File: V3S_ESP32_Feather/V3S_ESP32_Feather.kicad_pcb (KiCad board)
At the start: 4 copper layers, 30.5 x 48.3 mm, 83 parts, among them J1 USB_B_Micro, J10 UART, J2 PWM, J3 CAM, J5 U.FL-R-SMT(01), J7 Micro_SD_Card_Det, J8 I2C, J9 I2C, U1 V3S, U2 MIC5504-1.2YM5, U3 MIC5501-3.0YM5, U4 ICM-20948, U5 ESP32-PICO-D4, U6 LT1963AxST-3.3, U7 BMP280, U8 MIC5504-1.8YM5, U9 MAX13030EETE, Y1 X1E0000210832, Y2 CC5V-T1A 32.768KHZ +-20PPM 12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

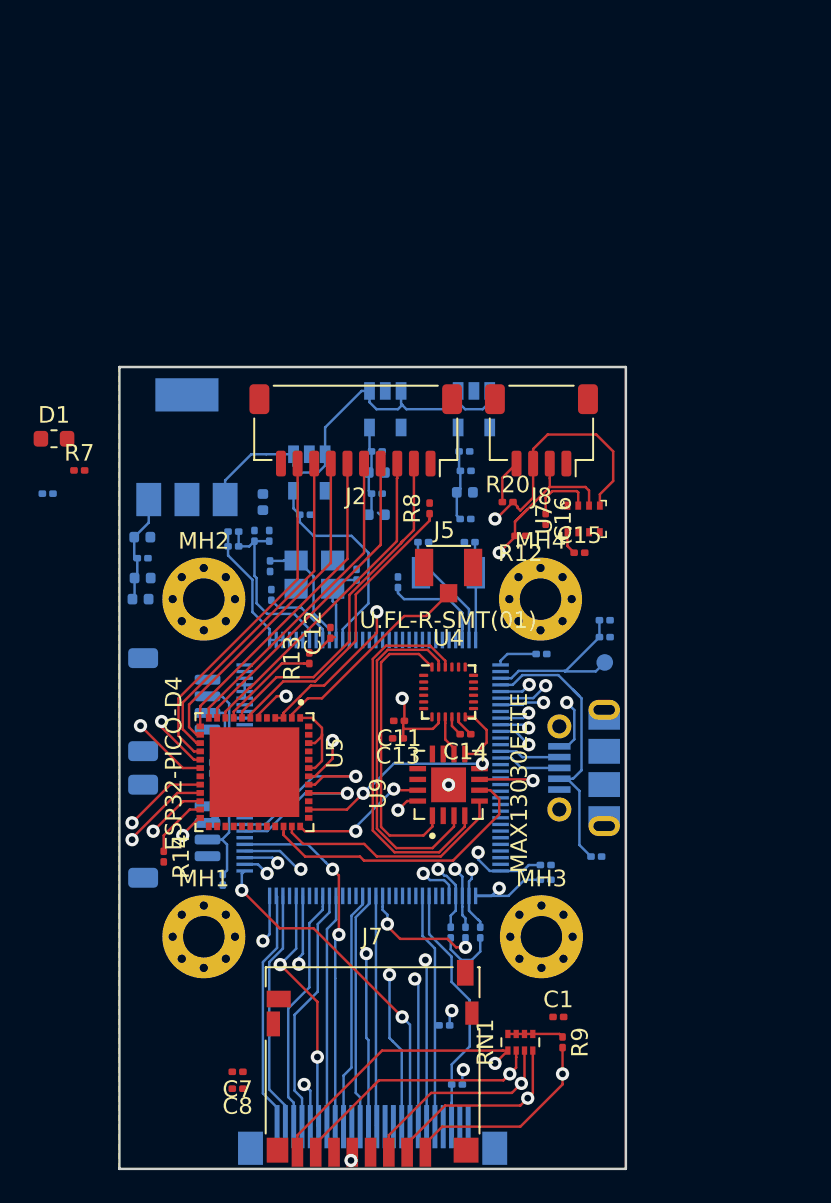
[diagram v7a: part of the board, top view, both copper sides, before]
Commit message: replace 3 ldo by 1, replace icm by mpu and progress on 2 layer
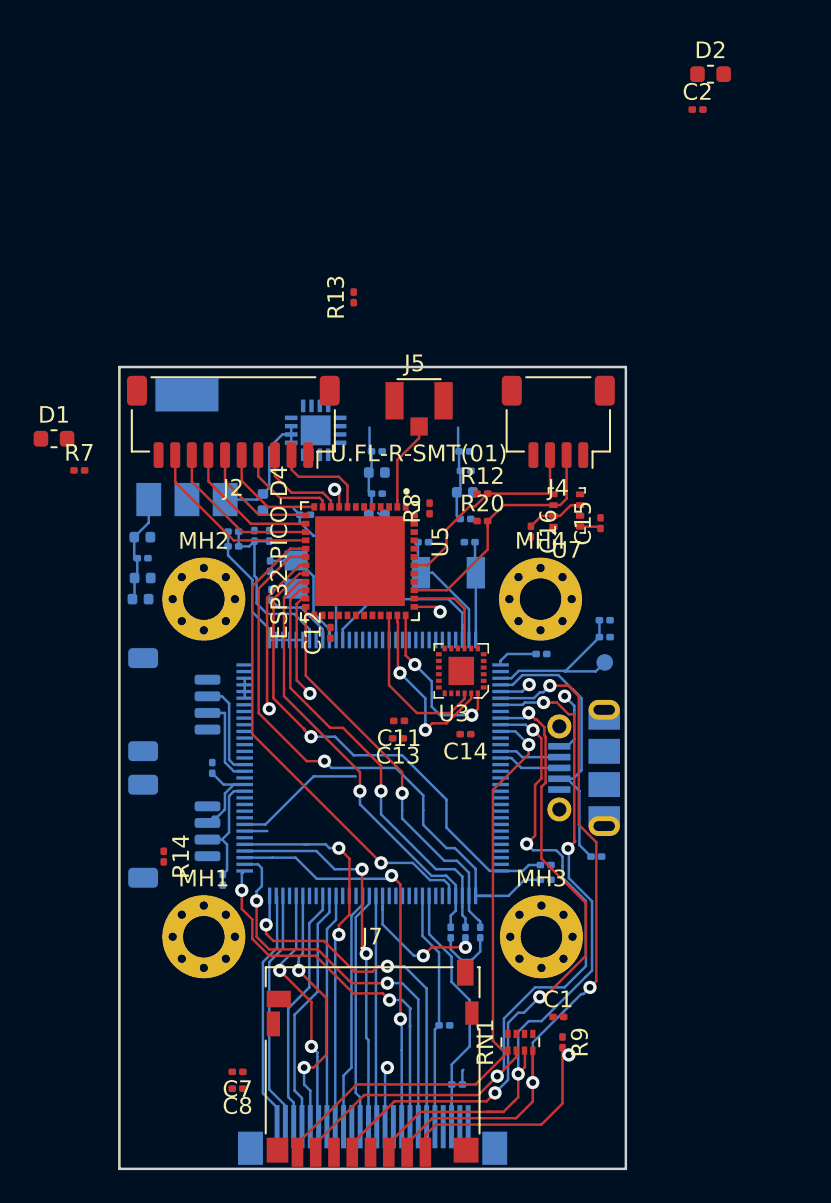
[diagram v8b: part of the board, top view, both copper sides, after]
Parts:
- removed J8: I2C, Connector_JST:JST_SH_SM04B-SRSS-TB_1x04-1MP_P1.00mm_Horizontal
- removed R1: 0, Resistor_SMD:R_0201_0603Metric
- removed U4: ICM-20948, Sensor_Motion:InvenSense_QFN-24_3x3mm_P0.4mm
- removed U8: MIC5504-1.8YM5, Package_TO_SOT_SMD:SOT-23-5
- removed U9: MAX13030EETE, MAX13035EETET:QFN65P400X400X80-17N
- added C2: 1uF, Capacitor_SMD:C_0201_0603Metric, F.Cu at (57.7, 4.83)
- added D2: D, Resistor_SMD:R_0603_1608Metric, F.Cu at (58.4, 2.70)
- added J4: I2C, Connector_JST:JST_SH_SM04B-SRSS-TB_1x04-1MP_P1.00mm_Horizontal, F.Cu at (49.3, 23.6)
- C11: value 0.1uF -> 10nF
- C13: value 1uF -> 0.1uF
- U2: value MIC5504-1.2YM5 -> ADP322ACPZ-145-R7; footprint Package_TO_SOT_SMD:SOT-23-5 -> QFN50P300X300X90-17N:QFN50P300X300X90-17N
- U3: value MIC5501-3.0YM5 -> MPU-9250_Obsolete; footprint Package_TO_SOT_SMD:SOT-23-5 -> digikey-footprints:QFN-24-1EP_3x3mm; moved to F.Cu
- moved R13 21.9 mm to (37.0, 16.1)
- moved U3 15.0 mm to (43.4, 38.6), turned to 180 degrees
- moved U5 14.2 mm to (37.3, 32.0)
- moved J5 10.2 mm to (40.9, 22.4)
- moved U2 9.61 mm to (34.7, 24.1), turned to 0 degrees
- moved J2 7.38 mm to (29.7, 23.6)
- moved R12 3.42 mm to (44.7, 27.9), turned to 0 degrees
- moved C15 2.18 mm to (51.8, 29.7), turned to 90 degrees
- moved R20 1.91 mm to (44.7, 29.6)
- moved C16 1.17 mm to (47.6, 30.2)
- moved U7 1.14 mm to (49.8, 29.0), turned to 180 degrees
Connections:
- net /IO25 renamed /WIFI, BT, RT/IO25
- net /IO26 renamed /WIFI, BT, RT/IO26
- net /IO27 renamed /WIFI, BT, RT/IO27
- net /IO32 renamed /WIFI, BT, RT/IO32
- net /IO33 renamed /WIFI, BT, RT/IO33
- net /IO34 renamed /WIFI, BT, RT/IO34
- net /IO35 renamed /WIFI, BT, RT/IO35
- net /SENSOR_VN renamed /WIFI, BT, RT/SENSOR_VN
- C11 pad 1: +1V8 -> +3V3
- C13 pad 1: +1V8 -> +3V3
- C5 pad 1: +BATT -> /PMIC Power Battery/VIN
- D1 pad 1: +BATT -> /PMIC Power Battery/VIN
- D1 pad 2: Net-(D1-Pad2) -> VBUS
- J3 pad 1: (no net) -> /All V3s input output/STROBE
- J3 pad 10: (no net) -> Net-(J3-Pad10)
- J7 pad 10: (no net) -> Net-(J7-Pad10)
- J7 pad 9: (no net) -> Net-(J7-Pad9)
- R12 pad 2: /SDA -> /WIFI, BT, RT/SCL
- R20 pad 2: /SCL -> /WIFI, BT, RT/SDA
- U1 pad 10: (no net) -> Net-(U1-Pad10)
- U1 pad 11: (no net) -> Net-(U1-Pad11)
- U1 pad 112: (no net) -> Net-(U1-Pad112)
- U1 pad 113: (no net) -> Net-(U1-Pad113)
- U1 pad 114: (no net) -> Net-(U1-Pad114)
- U1 pad 120: (no net) -> Net-(U1-Pad120)
- U1 pad 121: (no net) -> Net-(U1-Pad121)
- U1 pad 124: (no net) -> Net-(U1-Pad124)
- U1 pad 125: (no net) -> Net-(U1-Pad125)
- U1 pad 13: (no net) -> Net-(U1-Pad13)
- U1 pad 14: (no net) -> Net-(U1-Pad14)
- U1 pad 43: (no net) -> Net-(U1-Pad43)
- U1 pad 44: (no net) -> Net-(U1-Pad44)
- U1 pad 52: (no net) -> Net-(U1-Pad52)
- U1 pad 53: (no net) -> Net-(U1-Pad53)
- U1 pad 54: (no net) -> Net-(U1-Pad54)
- U1 pad 55: (no net) -> Net-(U1-Pad55)
- U1 pad 6: (no net) -> Net-(U1-Pad6)
- U1 pad 7: (no net) -> Net-(U1-Pad7)
- U1 pad 77: (no net) -> Net-(U1-Pad77)
- U1 pad 78: (no net) -> Net-(U1-Pad78)
- U1 pad 81: (no net) -> Net-(U1-Pad81)
- U1 pad 82: (no net) -> Net-(U1-Pad82)
- U1 pad 83: (no net) -> Net-(U1-Pad83)
- U1 pad 84: (no net) -> Net-(U1-Pad84)
- U1 pad 86: (no net) -> Net-(U1-Pad86)
- U1 pad 87: (no net) -> Net-(U1-Pad87)
- U1 pad 89: (no net) -> Net-(U1-Pad89)
- U1 pad 90: (no net) -> Net-(U1-Pad90)
- U1 pad 91: (no net) -> Net-(U1-Pad91)
- U1 pad 92: (no net) -> Net-(U1-Pad92)
- U2 pad 1: +BATT -> /PMIC Power Battery/VIN
- U2 pad 2: GND -> /PMIC Power Battery/VIN
- U2 pad 3: +BATT -> /PMIC Power Battery/VIN
- U2 pad 4: (no net) -> Net-(U2-Pad4)
- U2 pad 5: +1V2 -> +3V0
- U3 pad 1: +BATT -> +3V3
- U3 pad 2: GND -> Net-(U3-Pad2)
- U3 pad 3: +BATT -> Net-(U3-Pad3)
- U3 pad 4: (no net) -> Net-(U3-Pad4)
- U3 pad 5: +3V0 -> Net-(U3-Pad5)
- U5 pad 25: (no net) -> Net-(U5-Pad25)
- U5 pad 26: (no net) -> Net-(U5-Pad26)
- U5 pad 27: (no net) -> Net-(U5-Pad27)
- U5 pad 28: (no net) -> /WIFI, BT, RT/SD2
- U5 pad 29: (no net) -> /WIFI, BT, RT/SD3
- U5 pad 30: (no net) -> Net-(U5-Pad30)
- U5 pad 31: (no net) -> Net-(U5-Pad31)
- U5 pad 32: (no net) -> Net-(U5-Pad32)
- U5 pad 33: (no net) -> Net-(U5-Pad33)
- U5 pad 39: /SDA -> /WIFI, BT, RT/SDA
- U5 pad 42: /SCL -> /WIFI, BT, RT/SCL
- U5 pad 5: (no net) -> Net-(U5-Pad5)
- U6 pad 1: +BATT -> /PMIC Power Battery/VIN
- U7 pad 3: /SDA -> /WIFI, BT, RT/SDA
- U7 pad 4: /SCL -> /WIFI, BT, RT/SCL
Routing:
- net +BATT: track 26.5 -> 0.00 mm
- net /All V3s input output/PF5: track 41.8 -> 15.9 mm
- net /WIFI, BT, RT/CS1.8: track 23.1 -> 0.00 mm
- net /WIFI, BT, RT/CLK1.8: track 21.1 -> 0.00 mm
- net /SCL: track 18.4 -> 0.00 mm, vias 2 -> 0
- net Net-(R8-Pad1): track 17.9 -> 0.00 mm
- net /WIFI, BT, RT/MOSI1.8: track 17.7 -> 0.00 mm
- net /WIFI, BT, RT/SENSOR_VN: track 21.1 -> 5.93 mm
- net /WIFI, BT, RT/SDA: track 0.00 -> 15.1 mm
- net /WIFI, BT, RT/IO34: track 19.6 -> 5.62 mm
- net /WIFI, BT, RT/IO35: track 19.4 -> 6.13 mm
- net /WIFI, BT, RT/SCL: track 0.00 -> 13.2 mm
- net /WIFI, BT, RT/IO32: track 19.2 -> 6.57 mm
- net /WIFI, BT, RT/IO33: track 19.5 -> 7.28 mm
- net /WIFI, BT, RT/IO25: track 20.3 -> 8.49 mm
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- removed copper zone on In1.Cu, net GND
- removed copper zone on In2.Cu, net GND
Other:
- copper layers 4 -> 2
